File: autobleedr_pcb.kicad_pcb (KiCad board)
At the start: 2 copper layers, 102 x 86.5 mm, 19 parts, among them J1 Barrel_Jack, J10 XT60 Connector, J11 Conn_01x02_Pin, J2 Conn_01x13_Pin, J3 Conn_01x14_Pin, J4 Conn_01x08_Socket, J5 Conn_01x05_Pin, J6 Conn_01x05_Pin, J7 Screw_Terminal_01x02, J8 Conn_01x02_Pin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

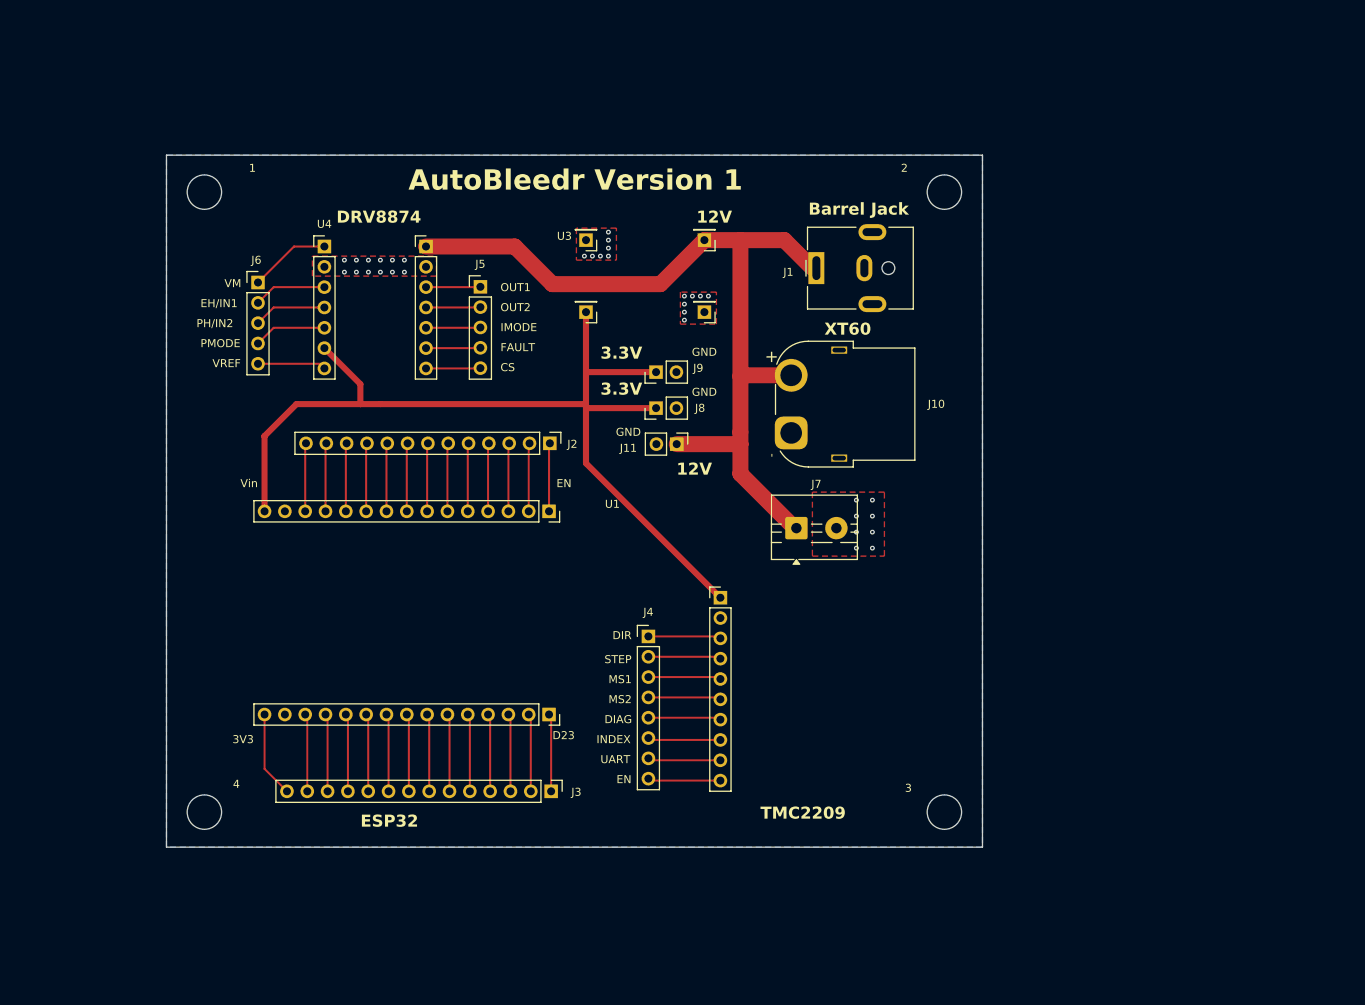
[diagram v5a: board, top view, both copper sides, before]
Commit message: updated pcb with DRV and working on compressing PCB itself:
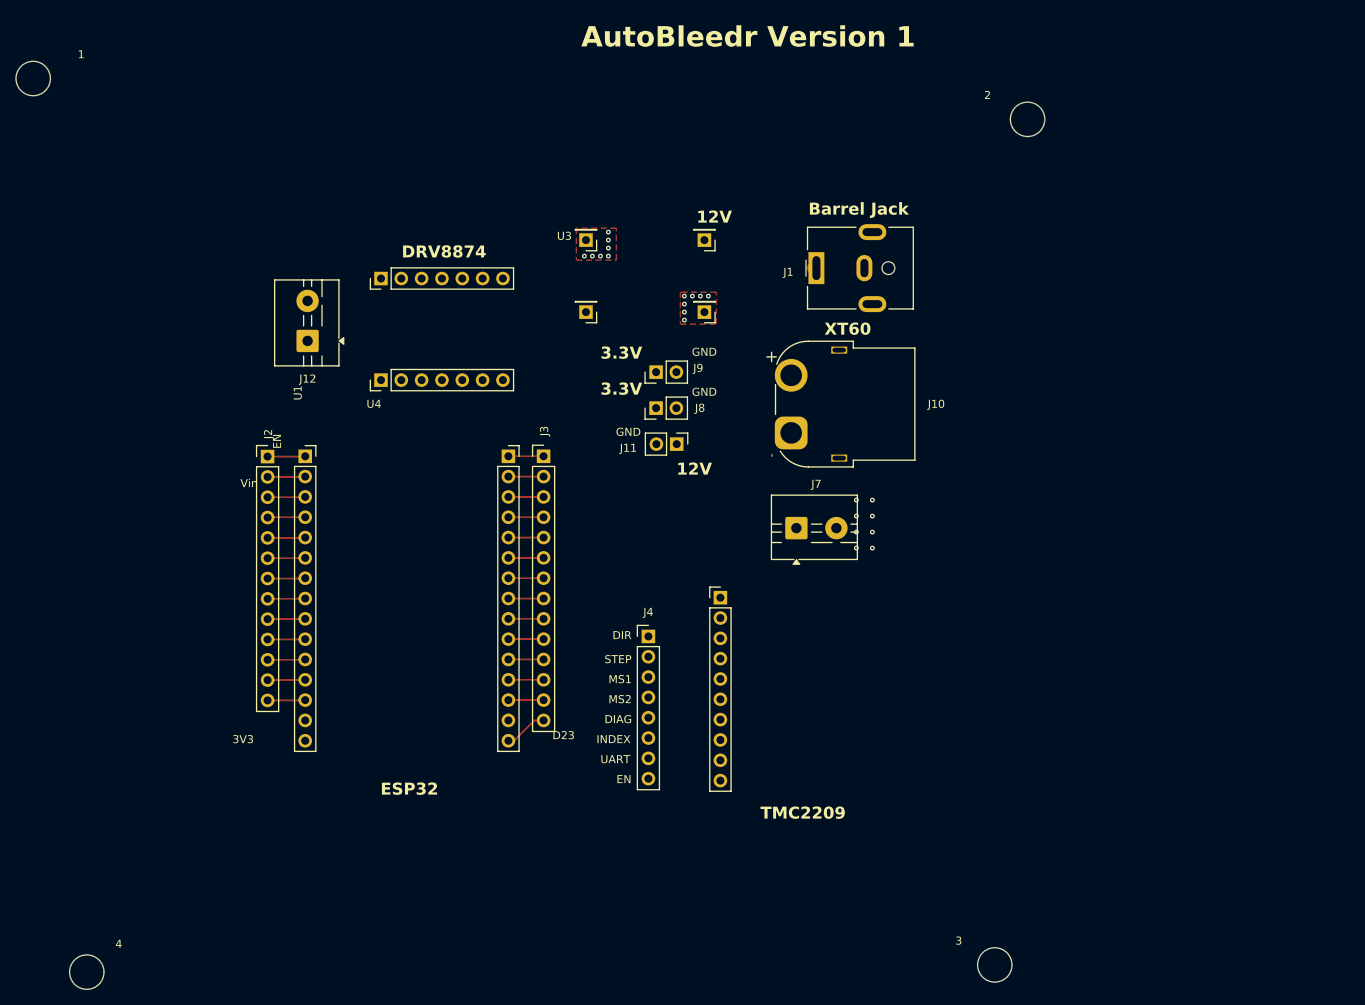
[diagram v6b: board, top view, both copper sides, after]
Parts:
- removed J5, J6: Conn_01x05_Pin, Connector_PinHeader_2.54mm:PinHeader_1x05_P2.54mm_Vertical
- added J12: Lin Actuator Screw Terminal, TerminalBlock:TerminalBlock_MaiXu_MX126-5.0-02P_1x02_P5.00mm, F.Cu at (81.4, 81.6)
- moved J3 41.9 mm to (110.9, 96.0), turned to 0 degrees
- moved J2 35.3 mm to (76.4, 96.1), turned to 0 degrees
- moved U1 31.2 mm to (81.1, 96.0), turned to 0 degrees
- moved 1 25.7 mm to (47.1, 48.8)
- moved 4 24.8 mm to (53.8, 160.5)
- moved 3 20.1 mm to (167.3, 159.6)
- moved U4 18.1 mm to (90.6, 86.5), turned to 90 degrees
- moved 2 13.8 mm to (171.4, 53.9)
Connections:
- J2 pad 7: Net-(J2-Pin_7) -> /linear actuator direction
- J2 pad 8: Net-(J2-Pin_8) -> /enable DRV
- U1 pad 7: Net-(J2-Pin_7) -> /linear actuator direction
- U1 pad 8: Net-(J2-Pin_8) -> /enable DRV
- U4 pad 10: Net-(J5-Pin_3) -> unconnected-(U4-IMODE-Pad10)
- U4 pad 3: Net-(J6-Pin_2) -> /enable DRV
- U4 pad 4: Net-(J6-Pin_3) -> /linear actuator direction
- U4 pad 5: Net-(J6-Pin_4) -> GND
- U4 pad 6: +3.3V -> /enable DRV
- U4 pad 8: Net-(J5-Pin_5) -> unconnected-(U4-CS-Pad8)
- U4 pad 9: Net-(J5-Pin_4) -> unconnected-(U4-FAULT-Pad9)
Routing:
- net +3.3V: track 120.3 -> 0.00 mm
- net +12V: track 107.0 -> 0.50 mm
- net unconnected-(U4-VM-Pad1): track 10.2 -> 0.00 mm
- net Net-(J6-Pin_4): track 9.11 -> 0.00 mm
- net Net-(J6-Pin_2): track 9.11 -> 0.00 mm
- net Net-(J6-Pin_3): track 9.11 -> 0.00 mm
- net Net-(J4-Pin_8): track 9.10 -> 0.34 mm
- net Net-(J4-Pin_7): track 9.10 -> 0.34 mm
- net Net-(J4-Pin_6): track 9.10 -> 0.34 mm
- net Net-(J4-Pin_4): track 9.44 -> 0.68 mm
- net Net-(J4-Pin_3): track 9.10 -> 0.34 mm
- net Net-(J4-Pin_2): track 9.10 -> 0.34 mm
- net Net-(J4-Pin_1): track 9.10 -> 0.34 mm
- net Net-(J4-Pin_5): track 9.44 -> 0.68 mm
- net Net-(J2-Pin_8): track 8.54 -> 0.00 mm
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- removed copper zone on B.Cu, net GND
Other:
- board outline removed
- copper layers 2 -> 4
- board text removed: "CS"
- board text removed: "EH/IN1"
- board text removed: "FAULT"
- board text removed: "IMODE"
- board text removed: "OUT1"
- board text removed: "OUT2"
- board text removed: "PH/IN2"
- board text removed: "PMODE"
- board text removed: "VREF"

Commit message: compressed PCB more
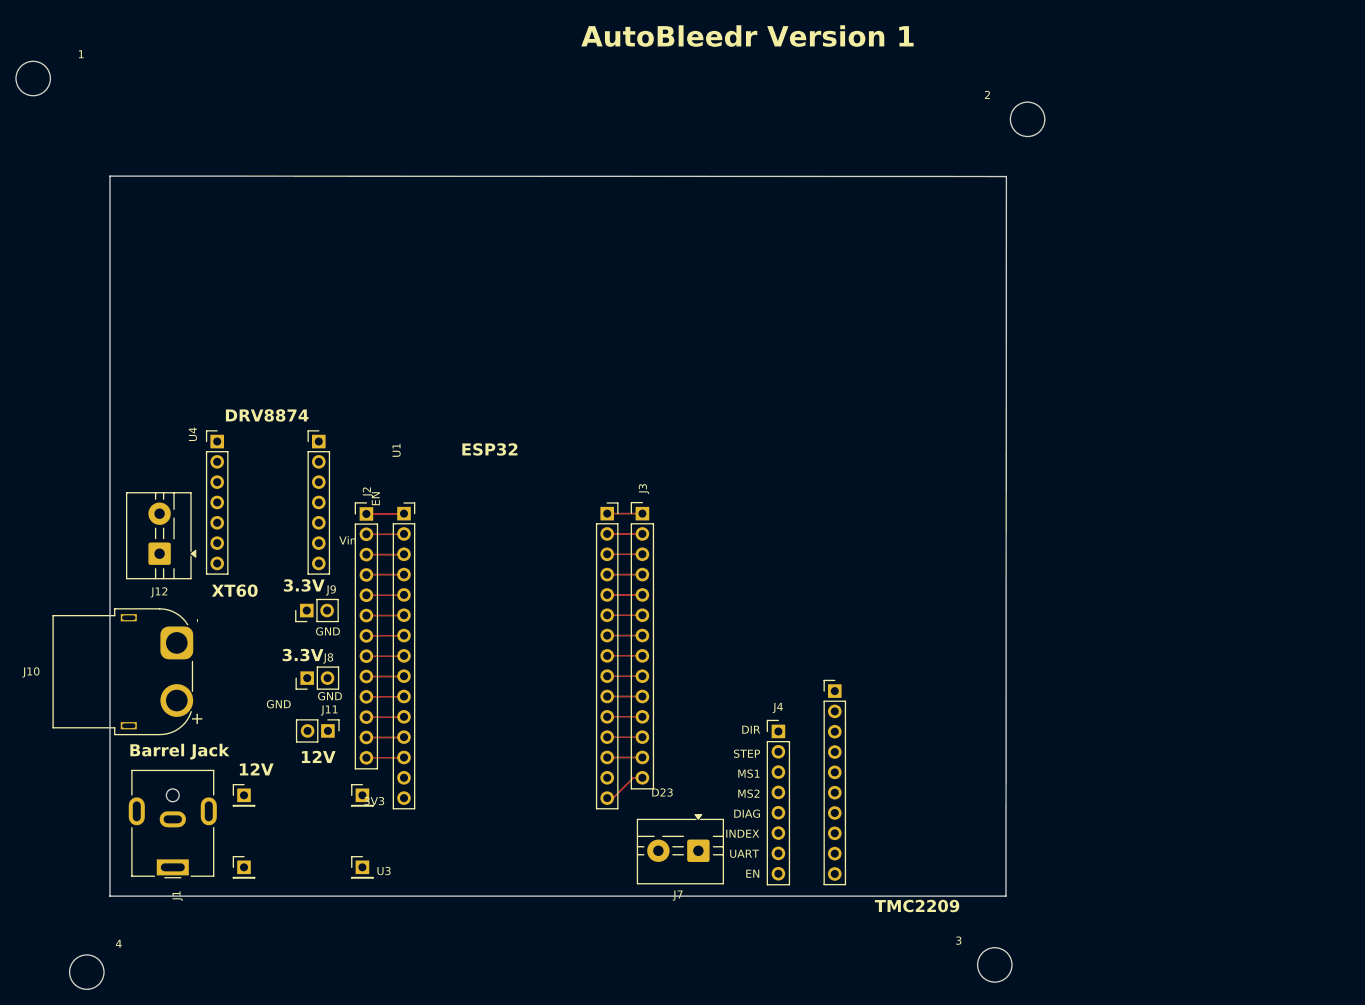
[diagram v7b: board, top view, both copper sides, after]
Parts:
- moved J1 109.9 mm to (64.5, 147.4), turned to 180 degrees
- moved U3 83.4 mm to (73.5, 138.4), turned to 0 degrees
- moved J10 81.2 mm to (65.0, 119.3), turned to 90 degrees
- moved J11 56.4 mm to (83.9, 130.3)
- moved J8 55.1 mm to (81.3, 123.8)
- moved J9 52.9 mm to (81.3, 115.3)
- moved J7 42.2 mm to (130.2, 145.3), turned to 180 degrees
- moved J12 32.4 mm to (62.9, 108.2)
- moved U4 21.9 mm to (70.1, 94.2), turned to 0 degrees
- moved J4 20.1 mm to (140.2, 130.4)
- moved U2 18.5 mm to (147.3, 135.5)
- moved U1 14.3 mm to (93.5, 103.2)
- moved J2 14.3 mm to (88.8, 103.2)
- moved J3 14.3 mm to (123.2, 103.2)
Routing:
- net Net-(J4-Pin_5): track 0.68 -> 0.00 mm
- net Net-(J4-Pin_4): track 0.68 -> 0.00 mm
- net +12V: track 0.50 -> 0.00 mm
- net GND: vias 22 -> 0
- removed copper zone on F.Cu, net GND
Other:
- board outline added: 112 x 90.1 mm

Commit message: Add files via upload
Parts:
- added 0.1uF_Bypass1: C, Capacitor_THT:C_Axial_L5.1mm_D3.1mm_P7.50mm_Horizontal, F.Cu at (128.8, 126.5)
- added 220_Ohm1: R, Resistor_THT:R_Axial_DIN0207_L6.3mm_D2.5mm_P7.62mm_Horizontal, F.Cu at (128.6, 116.5)
- added 330kOhm1: R, Resistor_THT:R_Axial_DIN0207_L6.3mm_D2.5mm_P7.62mm_Horizontal, F.Cu at (98.4, 89.0)
- added J5: IR LED, TerminalBlock:TerminalBlock_MaiXu_MX126-5.0-02P_1x02_P5.00mm, F.Cu at (130.5, 107.5)
- added J6: Photo Transistor, TerminalBlock:TerminalBlock_MaiXu_MX126-5.0-02P_1x02_P5.00mm, F.Cu at (99.5, 80.5)
- J12: value Lin Actuator Screw Terminal -> Linear Actuator Screw_Terminal_01x02
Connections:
- net Net-(J2-Pin_4) renamed D34
- net Net-(J3-Pin_13) renamed D15
- net Net-(J3-Pin_14) renamed 3V3
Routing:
- net 3V3: track 5.45 -> 0.00 mm
- net Net-(J2-Pin_13): track 4.72 -> 0.00 mm
- net unconnected-(J2-Pin_3-Pad3): track 4.72 -> 0.00 mm
- net Net-(J2-Pin_6): track 4.72 -> 0.00 mm
- net Net-(J2-Pin_5): track 4.72 -> 0.00 mm
- net Net-(J2-Pin_10): track 4.72 -> 0.00 mm
- net Net-(J2-Pin_1): track 4.72 -> 0.00 mm
- net /enable DRV: track 4.72 -> 0.00 mm
- net unconnected-(J2-Pin_2-Pad2): track 4.72 -> 0.00 mm
- net Net-(J2-Pin_9): track 4.72 -> 0.00 mm
- net Net-(J2-Pin_12): track 4.72 -> 0.00 mm
- net Net-(J2-Pin_11): track 4.72 -> 0.00 mm
- net D34: track 4.72 -> 0.00 mm
- net /linear actuator direction: track 4.72 -> 0.00 mm
- net Net-(J3-Pin_9): track 4.40 -> 0.00 mm
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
